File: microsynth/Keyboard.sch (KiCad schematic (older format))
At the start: 55 parts, among them J5 Conn_01x02_Male, Q1 BC182, Q2 BC182L, SW1-DRIFT1 DRIFT, SW9 TRIGGER, U1 RC4136, U2 TL072, U3 4011, U4 4016, U5 LF347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

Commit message: Replace dodgy parts 1458, 4136 & LF351s
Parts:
- removed U1: RC4136, Package_DIP:DIP-14_W7.62mm_LongPads, symbol microsynth-rescue:RC4136-Amplifier_Operational
- removed U2: TL072, Package_DIP:DIP-8_W7.62mm_LongPads, symbol Amplifier_Operational:TL072
- removed U5: LF347, Package_DIP:DIP-14_W7.62mm_LongPads, symbol microsynth-rescue:LF347-Amplifier_Operational
- removed U6: TL071, Package_DIP:DIP-8_W7.62mm_LongPads, symbol Amplifier_Operational:TL071
- added U1: RC4136, Package_DIP:DIP-14_W7.62mm_LongPads, symbol pe_microsynth:RC4136
- added U2: LM1458, Package_DIP:DIP-8_W7.62mm_LongPads, symbol pe_microsynth:LM1458
- added U5: LF347, Package_DIP:DIP-14_W7.62mm_LongPads, symbol pe_microsynth:LF347
- added U6: LF351, Package_DIP:DIP-8_W7.62mm_LongPads, symbol pe_microsynth:LF351

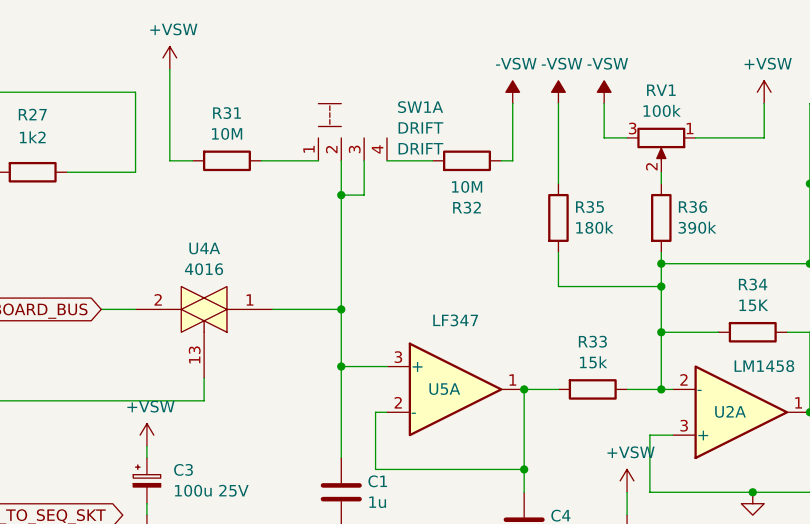
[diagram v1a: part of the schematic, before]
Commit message: Replace DP3T footprint, proper wire pads
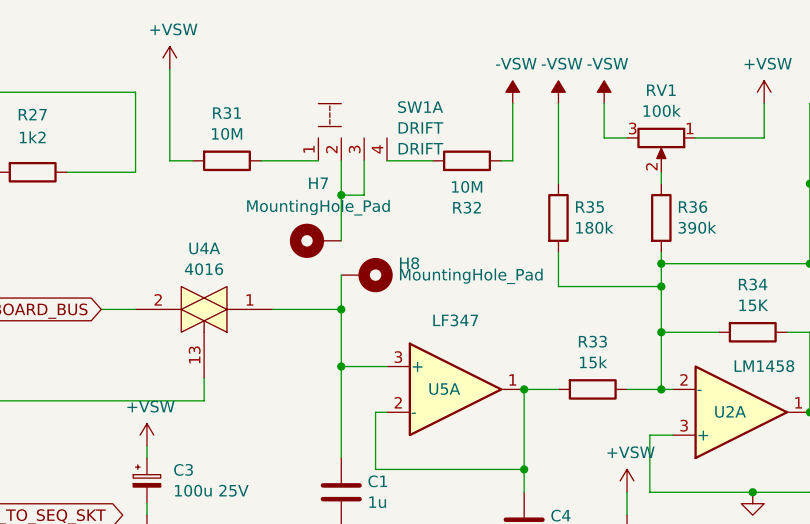
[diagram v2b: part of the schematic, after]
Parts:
- added H7, H8: MountingHole_Pad, Connector_PinHeader_2.54mm:PinHeader_1x01_P2.54mm_Vertical, symbol Mechanical:MountingHole_Pad
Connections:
- net at C1.1, U4.1, U5.3 (+): now also H8.1; no longer SW1-DRIFT1.2, SW1-DRIFT1.3
- new net: H7.1, SW1-DRIFT1.2, SW1-DRIFT1.3
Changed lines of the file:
@@
 	2150 2300 2150 2600
 Connection ~ 2150 2600
-Wire Wire Line
-	5600 2150 5600 1900
-Wire Wire Line
-	5600 1900 5300 1900
 Connection ~ 5600 2150
 $Comp
@@
 Wire Wire Line
 	5600 1250 5600 1400
-Connection ~ 5600 1900
 Wire Wire Line
 	5500 1250 5250 1250
@@
 	5700 1400 5600 1400
 Connection ~ 5600 1400
-Wire Wire Line
-	5600 1400 5600 1900
 $Comp
 L Device:R R32
@@
 $EndComp
 Connection ~ 6400 2250
+Wire Wire Line
+	5600 1400 5600 1600
+Wire Wire Line
+	5600 2150 5600 1900
+Connection ~ 5600 1900
+Wire Wire Line
+	5600 1900 5300 1900
+$Comp
+L Mechanical:MountingHole_Pad H7
+U 1 1 5EC658A5
+P 5500 1600
+F 0 "H7" V 5750 1600 50  0000 C CNN
+F 1 "MountingHole_Pad" V 5650 1600 50  0000 C CNN
+F 2 "Connector_PinHeader_2.54mm:PinHeader_1x01_P2.54mm_Vertical" H 5500 1600 50  0001 C CNN
+F 3 "~" H 5500 1600 50  0001 C CNN
+	1    5500 1600
+	0    -1   -1   0
+$EndComp
+$Comp
+L Mechanical:MountingHole_Pad H8
+U 1 1 5EC665D5
+P 5700 1750
+F 0 "H8" V 5650 1900 50  0000 L CNN
+F 1 "MountingHole_Pad" V 5700 1900 50  0000 L CNN
+F 2 "Connector_PinHeader_2.54mm:PinHeader_1x01_P2.54mm_Vertical" H 5700 1750 50  0001 C CNN
+F 3 "~" H 5700 1750 50  0001 C CNN
+	1    5700 1750
+	0    1    1    0
+$EndComp
+Wire Wire Line
+	5600 1750 5600 1900
 $EndSCHEMATC

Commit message: Consolidate switches
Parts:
- added R153: 1k, Resistor_THT:R_Axial_DIN0207_L6.3mm_D2.5mm_P10.16mm_Horizontal, symbol Device:R
- added SW1: SW_DP3T, microsynth:11-SS-23-832C, symbol pe_microsynth:SW_DPTT_SELECTOR-Switch
- SW1-DRIFT1: value DRIFT -> SW_DP3T; footprint Buttons_Switches_ThroughHole:G-1128S-1110 -> microsynth:11-SS-23-832C; symbol microsynth-rescue:SW_DPTT_SELECTOR-Switch -> pe_microsynth:SW_DPTT_SELECTOR-Switch
- SW9: value TRIGGER -> SW_DP3T; footprint Buttons_Switches_ThroughHole:G-1128S-1110 -> microsynth:11-SS-23-832C; Value (none) -> TRIGGER
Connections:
- net +VSW: now also R153.1; no longer SW9.2
- new net: R153.2, SW9.2
- no-connect marks 2 -> 6
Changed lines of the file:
@@
 	2600 3300 2600 3500
 Connection ~ 2400 3300
-Wire Wire Line
-	2500 3500 2500 3350
-Wire Wire Line
-	2500 3350 1850 3350
-Wire Wire Line
-	1850 3350 1850 3200
 $Comp
 L power:+VSW #PWR?
 U 1 1 5E8EF5B5
-P 1850 3200
-F 0 "#PWR?" H 1850 3050 50  0001 C CNN
-F 1 "+VSW" H 1865 3373 50  0000 C CNN
-F 2 "" H 1850 3200 50  0001 C CNN
-F 3 "" H 1850 3200 50  0001 C CNN
-	1    1850 3200
+P 1700 3200
+F 0 "#PWR?" H 1700 3050 50  0001 C CNN
+F 1 "+VSW" H 1715 3373 50  0000 C CNN
+F 2 "" H 1700 3200 50  0001 C CNN
+F 3 "" H 1700 3200 50  0001 C CNN
+	1    1700 3200
 	1    0    0    -1
 $EndComp
@@
 	4850 1250 4950 1250
 $Comp
-L microsynth-rescue:SW_DPTT_SELECTOR-Switch SW1-DRIFT1
+L pe_microsynth:SW_DPTT_SELECTOR-Switch SW1-DRIFT1
 U 1 1 5E91DC50
 P 5650 1050
@@
 AR Path="/5E8C1704/5E91DC50" Ref="SW1"  Part="1"
 F 0 "SW1" H 5844 1083 50  0000 L CNN
-F 1 "DRIFT" H 5844 992 50  0000 L CNN
-F 2 "Buttons_Switches_ThroughHole:G-1128S-1110" H 5650 1050 50  0001 C CNN
-F 3 "https://www.tme.eu/Document/aa2d40399ed88e2cc02320a01dfb97ce/OSseries.pdf" H 5650 1050 50  0001 C CNN
+F 1 "SW_DP3T" H 5844 992 50  0000 L CNN
+F 2 "microsynth:11-SS-23-832C" H 5650 1050 50  0001 C CNN
+F 3 "" H 5650 1050 50  0001 C CNN
 F 4 "DRIFT" H 5844 901 50  0000 L CNN "Label"
 	1    5650 1050
@@
 P 2550 3700
 F 0 "SW9" H 2750 3850 50  0000 L CNN
-F 1 "TRIGGER" H 2750 3750 50  0000 L CNN
-F 2 "Buttons_Switches_ThroughHole:G-1128S-1110" H 2550 3700 50  0001 C CNN
+F 1 "SW_DP3T" H 2750 3750 50  0000 L CNN
+F 2 "microsynth:11-SS-23-832C" H 2550 3700 50  0001 C CNN
 F 3 "" H 2550 3700 50  0001 C CNN
+F 4 "TRIGGER" H 2550 3700 50  0001 C CNN "Value"
 	1    2550 3700
 	1    0    0    1
@@
 Wire Wire Line
 	5600 1750 5600 1900
+$Comp
+L pe_microsynth:SW_DPTT_SELECTOR-Switch SW1
+U 2 1 5ED0BE61
+P 5650 950
+F 0 "SW1" H 5850 1150 50  0000 L CNN
+F 1 "SW_DP3T" H 5850 1050 50  0000 L CNN
+F 2 "microsynth:11-SS-23-832C" H 5650 950 50  0001 C CNN
+F 3 "" H 5650 950 50  0001 C CNN
+F 4 "DRIFT" H 5850 950 50  0000 L CNN "Value"
+	2    5650 950
+	1    0    0    -1
+$EndComp
+NoConn ~ 5500 750
+NoConn ~ 5600 750
+NoConn ~ 5700 750
+NoConn ~ 5800 750
+Wire Wire Line
+	2500 3500 2500 3400
+Wire Wire Line
+	2500 3400 2100 3400
+Wire Wire Line
+	1700 3200 1700 3400
+Wire Wire Line
+	1700 3400 1800 3400
+$Comp
+L Device:R R153
+U 1 1 5ED7FE8B
+P 1950 3400
+F 0 "R153" V 2150 3300 50  0000 L CNN
+F 1 "1k" V 2050 3350 50  0000 L CNN
+F 2 "Resistor_THT:R_Axial_DIN0207_L6.3mm_D2.5mm_P10.16mm_Horizontal" V 1880 3400 50  0001 C CNN
+F 3 "~" H 1950 3400 50  0001 C CNN
+	1    1950 3400
+	0    -1   -1   0
+$EndComp
 $EndSCHEMATC

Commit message: Consolidate all(?) switches
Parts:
- RV2: footprint 4ms_Potentiometer:Pot_16mm_NoDet_RV16AF-4A -> microsynth:Pot_16mm_NoDet_RV16AF-4A
- SW9: symbol microsynth-rescue:SW_DPTT_SELECTOR-Switch -> pe_microsynth:SW_DPTT_SELECTOR-Switch
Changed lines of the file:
@@
 F 0 "RV2" V 7835 2350 50  0000 C CNN
 F 1 "2MLOG" V 7744 2350 50  0000 C CNN
-F 2 "4ms_Potentiometer:Pot_16mm_NoDet_RV16AF-4A" H 7950 2350 50  0001 C CNN
+F 2 "microsynth:Pot_16mm_NoDet_RV16AF-4A" H 7950 2350 50  0001 C CNN
 F 3 "~" H 7950 2350 50  0001 C CNN
 F 4 "Glide" V 7653 2350 50  0000 C CNN "Label"
@@
 	4700 950  4700 1300
 $Comp
-L microsynth-rescue:SW_DPTT_SELECTOR-Switch SW9
+L pe_microsynth:SW_DPTT_SELECTOR-Switch SW9
 U 1 1 5E96003B
 P 2550 3700

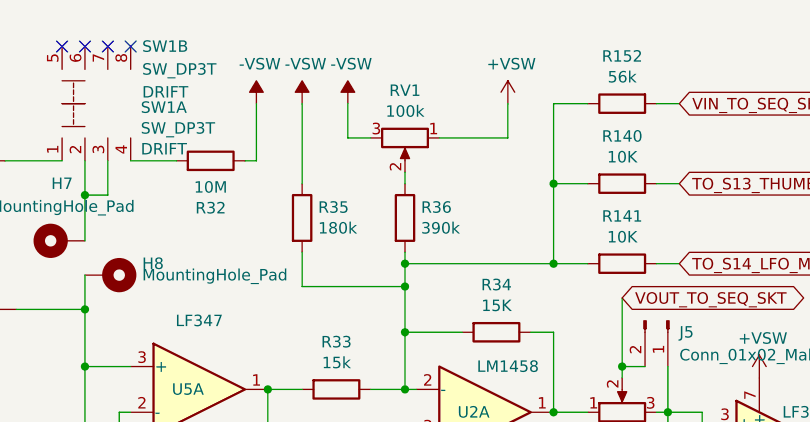
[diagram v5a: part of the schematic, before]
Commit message: Update image links, label Tune pot
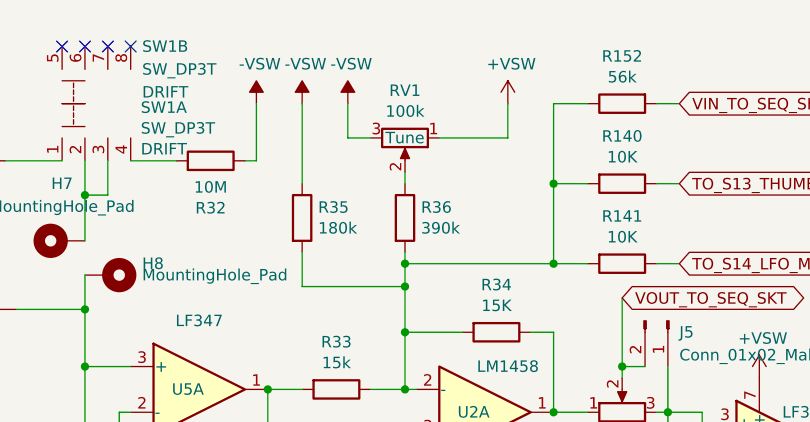
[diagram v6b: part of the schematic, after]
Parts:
- RV1: Label (none) -> Tune
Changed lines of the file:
@@
 F 2 "Potentiometers:Potentiometer_Trimmer_Bourns_PV36W" H 7000 1150 50  0001 C CNN
 F 3 "~" H 7000 1150 50  0001 C CNN
+F 4 "Tune" V 7000 1150 50  0000 C CNN "Label"
 	1    7000 1150
 	0    1    1    0

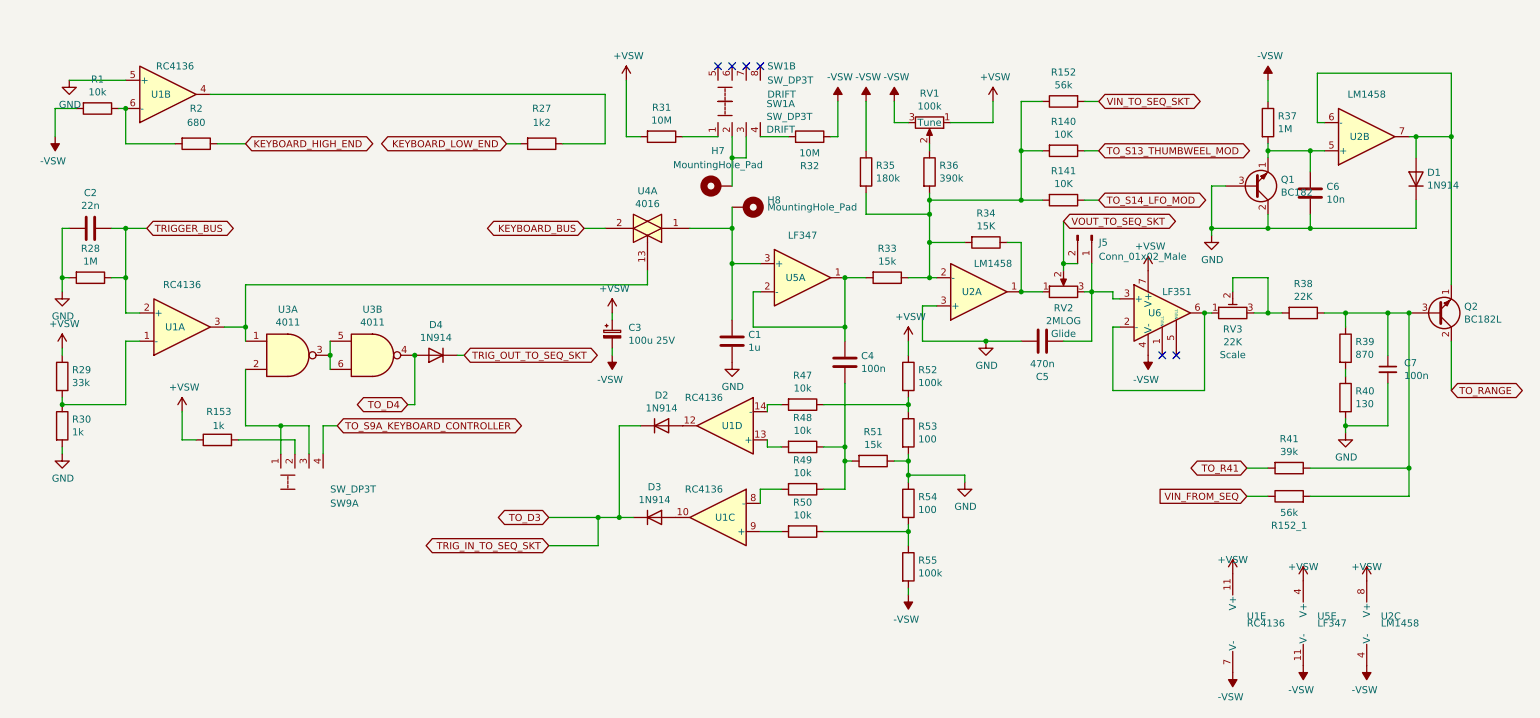
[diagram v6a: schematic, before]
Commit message: Replace IC1 with LM348, update component values
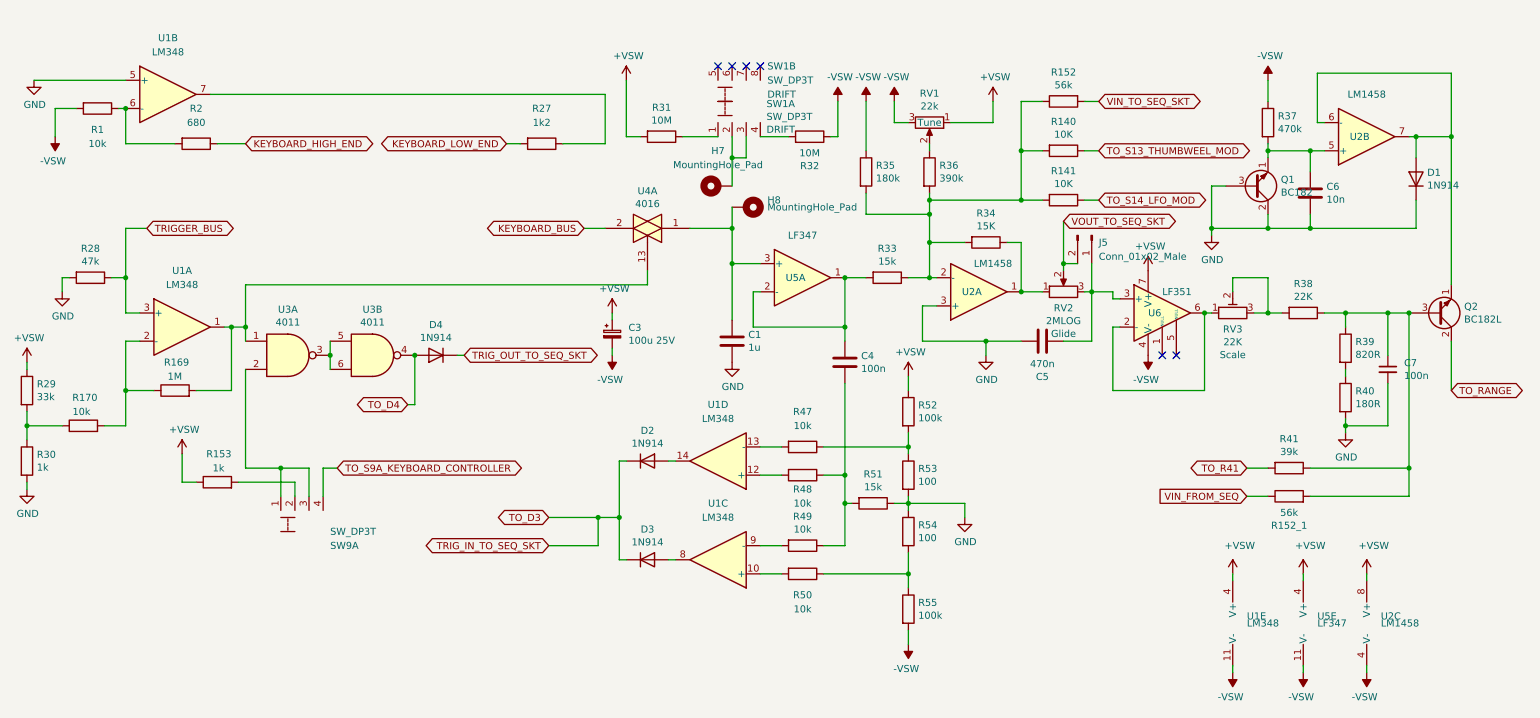
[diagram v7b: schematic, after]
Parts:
- removed C2: 22n, Capacitor_THT:C_Rect_L7.2mm_W2.5mm_P5.00mm_FKS2_FKP2_MKS2_MKP2, symbol Device:C
- removed U1: RC4136, Package_DIP:DIP-14_W7.62mm_LongPads, symbol pe_microsynth:RC4136
- added R169: 1M, Resistor_THT:R_Axial_DIN0207_L6.3mm_D2.5mm_P10.16mm_Horizontal, symbol Device:R
- added R170: 10k, Resistor_THT:R_Axial_DIN0207_L6.3mm_D2.5mm_P10.16mm_Horizontal, symbol Device:R
- added U1: LM348, Package_DIP:DIP-14_W7.62mm_LongPads, symbol pe_microsynth:LM348
- R28: value 1M -> 47k
- R37: value 1M -> 470k
- R39: value 870 -> 820R
- R40: value 130 -> 180R
- RV1: value 100k -> 22k
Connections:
- net +VSW: now also U1.4 (V+)
- net -VSW: now also U1.11 (V-)
- net GND: now also U1.5 (+)
- net TRIGGER_BUS: now also U1.3 (+)
- net at U3.1, U4.13: now also R169.2, U1.1
- net at R29.2, R30.1: now also R170.1
- net at R1.1, R2.2: now also U1.6 (-)
- net at R27.1: now also U1.7
- net at D3.2 (A): now also U1.8
- net at D2.2 (A): now also U1.14
- net at R47.2: now also U1.13 (-)
- net at R48.2: now also U1.12 (+)
- net at R49.2: now also U1.9 (-)
- net at R50.2: now also U1.10 (+)
- new net: R169.1, R170.2, U1.2 (-)
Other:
- moved on the sheet: D2, D3, R153, R29, R30, R47, R48, R49, R50, R51, R52, R53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

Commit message: Annotate schematic
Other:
- note added: "DOWN OFF UP"
- note added: "DRIFT"
- note added: "KBD RPT LFO"
- note added: "TRIGGER"
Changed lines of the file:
@@
 Wire Wire Line
 	7400 2800 7400 2700
+Text Notes 2400 3550 0    50   ~ 0
+KBD RPT LFO
+Text Notes 2700 4000 0    50   ~ 0
+TRIGGER
+Text Notes 5550 550  0    50   ~ 0
+DRIFT
+Text Notes 5350 700  0    50   ~ 0
+DOWN OFF UP
 $EndSCHEMATC
